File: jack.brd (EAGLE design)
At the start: 53.3 x 29.7 mm, 34 parts, among them IC1 NUF2221W1T2G, IC2 ATSAMD21G18, IC3 LDO, J1 USB-micro, SW1 SPST3.5X6MM, X1 CX-3225 12.288MHz

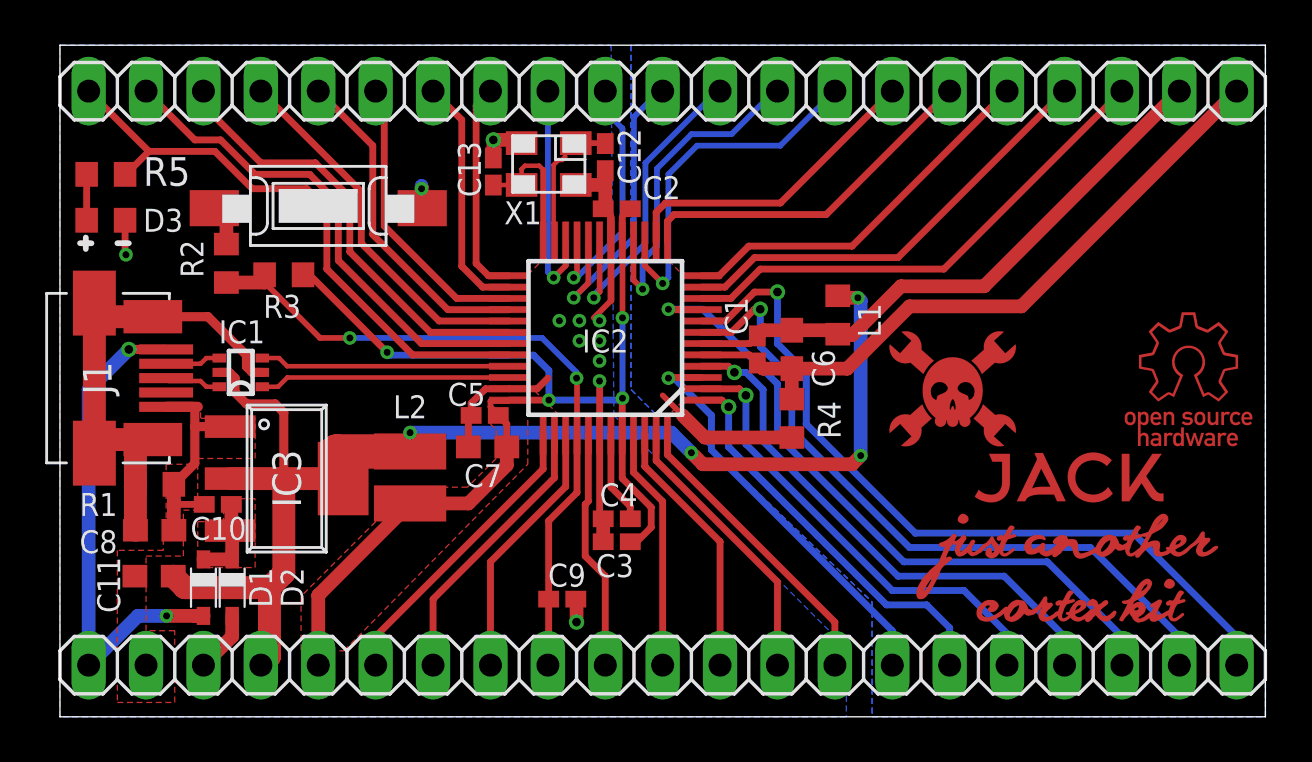
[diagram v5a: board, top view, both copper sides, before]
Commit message: :suspect: Revision 2! (pre-prototype fix)
Changed 10uF to polarized tantalum caps, changed packages accordingly,
had to move some stuff around, also had to add/resize some copper pours,
finally added polarity marks and place marks on all parts to give a more
detailed (readable) silk mask.
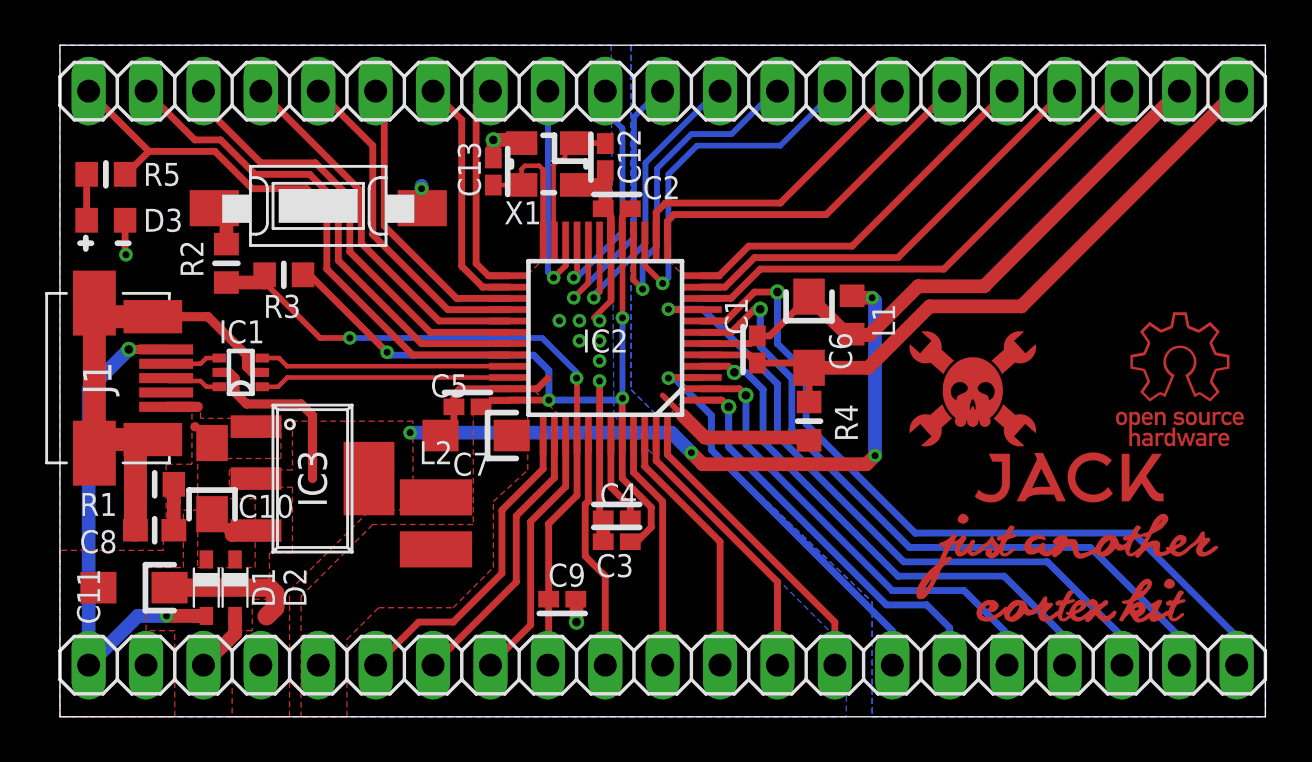
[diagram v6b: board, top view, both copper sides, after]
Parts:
- C10: device rcl:C0402K -> rcl:SMC_P
- C11, C6, C7: device rcl:C0603 -> rcl:SMC_P
- moved L2 2.33 mm to (16.6, 8.51)
- moved C10 1.17 mm to (6.73, 10.5), turned to 90 degrees
- moved IC3 1.14 mm to (11.2, 10.5)
- moved C6 1.08 mm to (33.1, 17.0)
- moved C11 1.02 mm to (3.28, 5.71)
- moved U$5 0.89 mm to (40.4, 14.1)
- moved C5 0.85 mm to (18.0, 13.7)
- moved R4 0.77 mm to (33.1, 13.1)
- moved C7 0.72 mm to (18.4, 12.4)
- moved L1 0.63 mm to (35.1, 17.8)
- moved U$6 0.38 mm to (49.5, 15.1)
- moved D1 0.13 mm to (6.48, 5.71)
- moved D2 0.13 mm to (7.75, 5.71)
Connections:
- net GND: now also C10.-, C11.-, C7.-; no longer C10.2, C11.2, C7.2
- net GNDANA: now also C6.-; no longer C6.2
- net LDOIN: now also C10.+; no longer C10.1
- net VDD: now also C11.+; no longer C11.1
- net VDDANA: now also C6.+; no longer C6.1
- net VDDF: now also C7.+; no longer C7.1
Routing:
- net VDDF: track 52.9 -> 35.9 mm
- net VDD: track 59.2 -> 43.3 mm
- net GND: track 46.6 -> 41.9 mm
- net VDDANA: track 26.0 -> 27.4 mm
- net 37: track 13.3 -> 14.2 mm
- added copper zone on layer 1, net VDD

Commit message: :sleepy: Reduced board size!
I managed to shrink the board in less than 3X5 cm^2. It now features an
8 pin header on the left side so to let the board fit under 5 cm on both
sides, to get cheapest PCB manufactury.
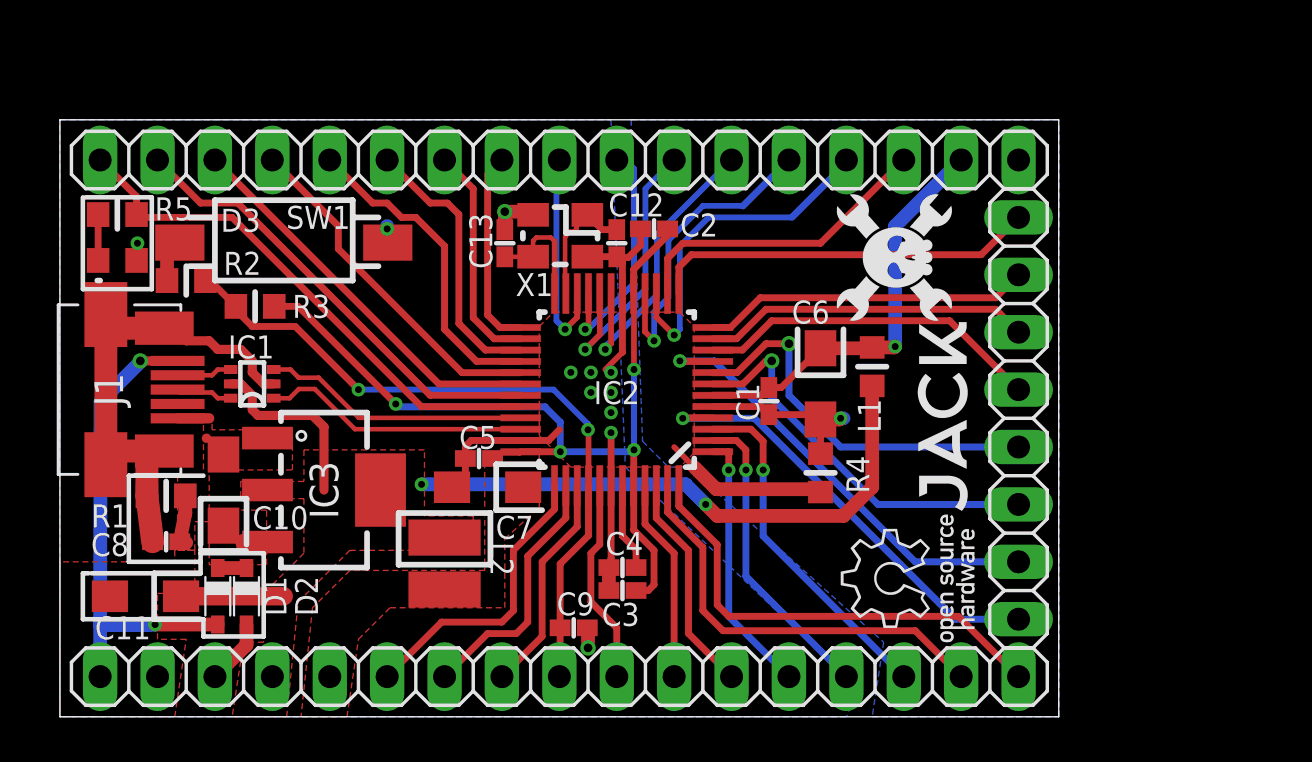
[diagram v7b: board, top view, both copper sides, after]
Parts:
- added JP3: (no value), pinhead:1X08
- C1, C12, C13, C2, C3, C5, C9: device rcl:C0402K -> jack:C0402K
- C10, C11, C6, C7: device rcl:SMC_P -> jack:SMC_P
- C8: device rcl:C0603 -> jack:C0402K
- JP1, JP2: value PINHD-1X21 -> (none); device jack:1X21 -> pinhead:1X17
- R1, R2, R3, R4, R5: device rcl:R0603 -> jack:R0603
- moved U$6 15.2 mm to (37.3, 6.10), turned to 90 degrees
- moved U$3 8.09 mm to (39.1, 13.2), turned to 90 degrees
- moved U$5 6.93 mm to (37.3, 20.3), turned to 90 degrees
- moved JP2 5.49 mm to (22.1, 24.6)
- moved JP1 4.60 mm to (22.1, 1.78)
- moved C12 3.84 mm to (24.6, 21.0)
- moved C13 3.22 mm to (19.7, 21.0)
- moved X1 3.22 mm to (22.1, 21.3)
- moved L1 2.45 mm to (35.9, 15.5), turned to 90 degrees
- moved C6 2.34 mm to (33.7, 14.7)
- moved C5 2.34 mm to (18.5, 11.4)
- moved IC2 2.34 mm to (24.6, 14.5)
- moved R4 2.34 mm to (33.7, 10.8)
- moved C1 2.34 mm to (31.4, 14.0)
- moved C7 2.34 mm to (18.9, 10.2)
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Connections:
- net !RESET: now also JP1.9; no longer JP1.13
- net 1: now also JP1.5; no longer JP1.6
- net 10: now also JP3.5; no longer JP2.19
- net 11: now also JP3.6; no longer JP2.18
- net 12: now also JP3.7; no longer JP2.17
- net 13: now also JP3.8; no longer JP2.16
- net 2: now also JP1.4; no longer JP1.5
- net 3: now also JP1.3; no longer JP1.7
- net 37: now also JP1.12; no longer JP1.16
- net 38: now also JP1.11; no longer JP1.15
- net 39: now also JP1.10; no longer JP1.14
- net 4: now also JP3.1; no longer JP1.4
- net 41: now also JP1.8; no longer JP1.12
- net 47: now also JP1.2; no longer JP1.9
- net 48: now also JP1.1; no longer JP1.8
- net 7: now also JP3.3; no longer JP1.2
- net 8: now also JP3.4; no longer JP1.1
- net 9: now also JP3.2; no longer JP1.3
- net GND: now also JP1.16; no longer JP1.20
- net GNDANA: now also JP2.17; no longer JP2.21
- net SWCLK: now also JP1.7; no longer JP1.11
- net SWDIO: now also JP1.6; no longer JP1.10
- net VBUS: now also JP1.17; no longer JP1.21
- net VDD: now also JP1.14; no longer JP1.18
- net VDDANA: now also JP2.16; no longer JP2.20
- net VDDF: now also JP1.13; no longer JP1.17
- net VIN: now also JP1.15; no longer JP1.19
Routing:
- net GNDANA: track 30.5 -> 7.55 mm, vias 0 -> 1
- net 8: track 34.7 -> 17.5 mm
- net 7: track 31.1 -> 17.5 mm
- net 9: track 30.3 -> 20.3 mm
- net VDDANA: track 27.4 -> 18.4 mm, vias 0 -> 1
- net 2: track 20.9 -> 13.5 mm
- net 48: track 13.3 -> 20.6 mm
- net 10: track 22.4 -> 15.3 mm
- net 47: track 12.5 -> 18.8 mm
- net 1: track 18.0 -> 11.8 mm
- net 11: track 19.7 -> 14.5 mm
- net VDD: track 43.3 -> 38.2 mm, vias 4 -> 2
- net VDDF: track 35.9 -> 39.7 mm
- net 4: track 23.6 -> 19.9 mm
- net 3: track 18.4 -> 15.4 mm
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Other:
- board size 53.3 x 29.7 mm -> 44.2 x 26.4 mm

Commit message: Minor changes (added BOM)
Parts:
- C10: value 100nF -> 10uF
- C4: device rcl:C0402K -> jack:C0402K
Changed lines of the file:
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@@
 <layer number="45" name="Holes" color="7" fill="1" visible="no" active="yes"/>
 <layer number="46" name="Milling" color="3" fill="1" visible="no" active="yes"/>
-<layer number="47" name="Measures" color="7" fill="1" visible="no" active="yes"/>
+<layer number="47" name="Measures" color="7" fill="1" visible="yes" active="yes"/>
 <layer number="48" name="Document" color="7" fill="1" visible="no" active="yes"/>
 <layer number="49" name="Reference" color="7" fill="1" visible="no" active="yes"/>
 <layer number="50" name="dxf" color="7" fill="1" visible="no" active="no"/>
-<layer number="51" name="tDocu" color="15" fill="1" visible="no" active="yes"/>
+<layer number="51" name="tDocu" color="15" fill="1" visible="yes" active="yes"/>
 <layer number="52" name="bDocu" color="7" fill="1" visible="no" active="yes"/>
 <layer number="53" name="tGND_GNDA" color="7" fill="1" visible="no" active="no"/>
@@
 <attribute name="VALUE" x="29.919" y="14.47" size="1.016" layer="27" rot="R270"/>
 </element>
-<element name="C10" library="jack" package="SMC_P" value="100nF" x="7.239" y="10.033" smashed="yes" rot="R90">
+<element name="C10" library="jack" package="SMC_P" value="10uF" x="7.239" y="10.033" smashed="yes" rot="R90">
 <attribute name="NAME" x="8.517" y="8.299" size="1.016" layer="25"/>
 <attribute name="VALUE" x="8.689" y="9.533" size="1.016" layer="27" rot="R90"/>
@@
 <attribute name="VALUE" x="25.392" y="7.038" size="1.016" layer="27" rot="R180"/>
 </element>
-<element name="C4" library="rcl" package="C0402K" value="100nF" x="24.892" y="6.604" smashed="yes" rot="R180">
+<element name="C4" library="jack" package="C0402K" value="100nF" x="24.892" y="6.604" smashed="yes" rot="R180">
 <attribute name="NAME" x="24.138" y="7.156" size="1.016" layer="25"/>
 <attribute name="VALUE" x="25.392" y="8.054" size="1.016" layer="27" rot="R180"/>
@@
 <vertex x="0" y="6.858"/>
 <vertex x="0" y="0"/>
-<vertex x="5.08" y="0"/>
+<vertex x="5.588" y="0"/>
 <vertex x="5.588" y="3.429"/>
 <vertex x="4.318" y="3.429"/>
@@
 <vertex x="9.017" y="3.302"/>
 <vertex x="8.128" y="3.302"/>
-<vertex x="7.62" y="0"/>
-<vertex x="10.033" y="0"/>
+<vertex x="8.128" y="0"/>
+<vertex x="10.541" y="0"/>
 <vertex x="10.541" y="5.08"/>
 <vertex x="12.827" y="7.366"/>
@@
 <contactref element="L1" pad="2"/>
 <wire x1="28.888" y1="14.228" x2="31.027" y2="14.228" width="0.3048" layer="1"/>
-<wire x1="31.369" y1="14.57" x2="31.918" y2="14.57" width="0.3048" layer="1"/>
-<wire x1="31.918" y1="14.57" x2="33.655" y2="16.307" width="0.3048" layer="1"/>
 <wire x1="31.027" y1="14.228" x2="31.369" y2="14.57" width="0.3048" layer="1"/>
-<wire x1="33.655" y1="16.307" x2="35.904" y2="16.307" width="0.6096" layer="1"/>
-<wire x1="35.904" y1="16.307" x2="35.941" y2="16.344" width="0.6096" layer="1"/>
 <contactref element="JP2" pad="16"/>
-<wire x1="35.941" y1="16.344" x2="36.918" y2="16.344" width="0.6096" layer="1"/>
-<wire x1="36.918" y1="16.344" x2="36.957" y2="16.383" width="0.6096" layer="1"/>
 <via x="36.957" y="16.383" extent="1-16" drill="0.3048" diameter="0.6096"/>
-<wire x1="36.957" y1="16.383" x2="36.957" y2="21.717" width="0.6096" layer="16"/>
-<wire x1="36.957" y1="21.717" x2="39.878" y2="24.638" width="0.6096" layer="16"/>
+<wire x1="31.369" y1="14.57" x2="31.918" y2="14.57" width="0.8128" layer="1"/>
+<wire x1="31.918" y1="14.57" x2="33.655" y2="16.307" width="0.8128" layer="1"/>
+<wire x1="33.655" y1="16.307" x2="35.904" y2="16.307" width="0.8128" layer="1"/>
+<wire x1="35.904" y1="16.307" x2="35.941" y2="16.344" width="0.8128" layer="1"/>
+<wire x1="35.941" y1="16.344" x2="36.918" y2="16.344" width="0.8128" layer="1"/>
+<wire x1="36.918" y1="16.344" x2="36.957" y2="16.383" width="0.8128" layer="1"/>
+<wire x1="36.957" y1="16.383" x2="36.957" y2="21.336" width="0.8128" layer="16"/>
+<wire x1="36.957" y1="21.336" x2="39.624" y2="24.003" width="0.8128" layer="16"/>
+<wire x1="39.624" y1="24.003" x2="39.624" y2="24.384" width="0.8128" layer="16"/>
+<wire x1="39.624" y1="24.384" x2="39.878" y2="24.638" width="0.8128" layer="16"/>
 </signal>
 <signal name="D+OUT">
@@
 <vertex x="12.827" y="6.477"/>
 <vertex x="11.176" y="4.826"/>
-<vertex x="10.668" y="0"/>
-<vertex x="12.7" y="0"/>
+<vertex x="11.176" y="0"/>
+<vertex x="13.208" y="0"/>
 <vertex x="13.208" y="3.429"/>
 <vertex x="14.605" y="4.826"/>
@@
 </polygon>
 <wire x1="33.442" y1="13.37" x2="33.655" y2="13.157" width="0.3048" layer="1"/>
-<wire x1="33.655" y1="11.645" x2="33.655" y2="13.157" width="0.3048" layer="1"/>
-<wire x1="31.369" y1="13.37" x2="33.442" y2="13.37" width="0.3048" layer="1"/>
 <wire x1="31.011" y1="13.728" x2="31.369" y2="13.37" width="0.3048" layer="1"/>
 <wire x1="33.655" y1="13.157" x2="34.493" y2="13.157" width="0.6096" layer="1"/>
@@
 <wire x1="34.544" y1="13.208" x2="34.671" y2="13.208" width="0.6096" layer="16"/>
 <contactref element="JP2" pad="17"/>
+<wire x1="33.655" y1="11.645" x2="33.655" y2="13.157" width="0.8128" layer="1"/>
+<wire x1="31.369" y1="13.37" x2="33.655" y2="13.37" width="0.8128" layer="1"/>
+<wire x1="33.655" y1="13.37" x2="33.655" y2="13.157" width="0.8128" layer="1"/>
 </signal>
 <signal name="SWCLK">
